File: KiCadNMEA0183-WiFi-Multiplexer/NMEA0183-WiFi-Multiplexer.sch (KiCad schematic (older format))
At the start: 11 parts, among them J1 NMEA In, J2 NMEA In, Q1 BC547, Q2 BC547, U1 WeMos_D1_mini

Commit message: Add files via upload
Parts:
- removed D1, D2: 1N4148, Diode_THT:D_DO-35_SOD27_P7.62mm_Horizontal, symbol Diode:1N4148
- removed Q1, Q2: BC547, Package_TO_SOT_THT:TO-92_Inline, symbol Transistor_BJT:BC547
- removed R1, R2: 33K, symbol Device:R
- removed R3, R4: 10K, symbol Device:R
- added C1, C2, C3, C4: 1µ, symbol Device:CP
- added U2: MAX232, symbol Interface_UART:MAX232
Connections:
- net GND is gone; now on an unnamed net: J1.1 (Pin_1), U1.10 (GND)
- net at U1.6 (MOSI/D7): now also U2.12 (R1OUT)
- net at U1.7 (CS/D8): now also U2.9 (R2OUT)
- net at U1.9 (5V): now also U2.16 (VCC)
- net at J1.2 (Pin_2): now also U2.8 (R2IN)
- net at J2.1 (Pin_1): now also C1.2, C3.1, U2.15 (GND)
- net at J2.2 (Pin_2): now also U2.13 (R1IN)
- new net: C4.1, U2.1 (C1+)
- new net: C1.1, U2.2 (VS+)
- new net: C4.2, U2.3 (C1-)
- new net: C2.1, U2.4 (C2+)
- new net: C2.2, U2.5 (C2-)
- new net: C3.2, U2.6 (VS-)
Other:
- moved on the sheet: J1, J2, U1
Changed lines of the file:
@@
 L MCU_Module:WeMos_D1_mini U1
 U 1 1 604342F8
-P 6100 3950
-F 0 "U1" H 6100 4900 50  0000 C CNN
-F 1 "WeMos_D1_mini" H 6100 5000 50  0000 C CNN
-F 2 "Module:WEMOS_D1_mini_light" H 6100 2800 50  0001 C CNN
-F 3 "https://wiki.wemos.cc/products:d1:d1_mini#documentation" H 4250 2800 50  0001 C CNN
-	1    6100 3950
+P 7050 4100
+F 0 "U1" H 7050 5050 50  0000 C CNN
+F 1 "WeMos_D1_mini" H 7050 5150 50  0000 C CNN
+F 2 "Module:WEMOS_D1_mini_light" H 7050 2950 50  0001 C CNN
+F 3 "https://wiki.wemos.cc/products:d1:d1_mini#documentation" H 5200 2950 50  0001 C CNN
+	1    7050 4100
 	-1   0    0    -1
-$EndComp
-$Comp
-L Transistor_BJT:BC547 Q1
-U 1 1 6043679E
-P 4850 4550
-F 0 "Q1" H 5041 4596 50  0000 L CNN
-F 1 "BC547" H 5041 4505 50  0000 L CNN
-F 2 "Package_TO_SOT_THT:TO-92_Inline" H 5050 4475 50  0001 L CIN
-F 3 "http://www.fairchildsemi.com/ds/BC/BC547.pdf" H 4850 4550 50  0001 L CNN
-	1    4850 4550
-	1    0    0    -1
-$EndComp
-$Comp
-L Device:R R1
-U 1 1 60437DBF
-P 4300 4550
-F 0 "R1" V 4093 4550 50  0000 C CNN
-F 1 "33K" V 4184 4550 50  0000 C CNN
-F 2 "" V 4230 4550 50  0001 C CNN
-F 3 "~" H 4300 4550 50  0001 C CNN
-	1    4300 4550
-	0    1    1    0
 $EndComp
 $Comp
 L Connector_Generic:Conn_01x02 J1
 U 1 1 60439978
-P 3800 4650
-F 0 "J1" H 3718 4325 50  0000 C CNN
-F 1 "NMEA In" H 3718 4416 50  0000 C CNN
-F 2 "" H 3800 4650 50  0001 C CNN
-F 3 "~" H 3800 4650 50  0001 C CNN
-	1    3800 4650
+P 1650 4600
+F 0 "J1" H 1568 4275 50  0000 C CNN
+F 1 "NMEA In" H 1568 4366 50  0000 C CNN
+F 2 "" H 1650 4600 50  0001 C CNN
+F 3 "~" H 1650 4600 50  0001 C CNN
+	1    1650 4600
 	-1   0    0    1
-$EndComp
-Wire Wire Line
-	4000 4550 4150 4550
-Wire Wire Line
-	4950 4350 5700 4350
-Wire Wire Line
-	4450 4550 4550 4550
-Wire Wire Line
-	4550 4650 4550 4550
-Connection ~ 4550 4550
-Wire Wire Line
-	4550 4550 4650 4550
-$Comp
-L power:GND #PWR01
-U 1 1 6043BBF4
-P 6100 4950
-F 0 "#PWR01" H 6100 4700 50  0001 C CNN
-F 1 "GND" H 6105 4777 50  0000 C CNN
-F 2 "" H 6100 4950 50  0001 C CNN
-F 3 "" H 6100 4950 50  0001 C CNN
-	1    6100 4950
-	1    0    0    -1
-$EndComp
-Wire Wire Line
-	6100 4750 6100 4950
-$Comp
-L Device:R R4
-U 1 1 6044381A
-P 4950 4200
-F 0 "R4" H 5020 4246 50  0000 L CNN
-F 1 "10K" H 5020 4155 50  0000 L CNN
-F 2 "" V 4880 4200 50  0001 C CNN
-F 3 "~" H 4950 4200 50  0001 C CNN
-	1    4950 4200
-	1    0    0    -1
-$EndComp
-Connection ~ 4950 4350
-Connection ~ 6100 4950
-$Comp
-L Transistor_BJT:BC547 Q2
-U 1 1 6043EAEA
-P 4850 3450
-F 0 "Q2" H 5041 3496 50  0000 L CNN
-F 1 "BC547" H 5041 3405 50  0000 L CNN
-F 2 "Package_TO_SOT_THT:TO-92_Inline" H 5050 3375 50  0001 L CIN
-F 3 "http://www.fairchildsemi.com/ds/BC/BC547.pdf" H 4850 3450 50  0001 L CNN
-	1    4850 3450
-	1    0    0    -1
-$EndComp
-$Comp
-L Device:R R2
-U 1 1 6043EAF4
-P 4300 3450
-F 0 "R2" V 4093 3450 50  0000 C CNN
-F 1 "33K" V 4184 3450 50  0000 C CNN
-F 2 "" V 4230 3450 50  0001 C CNN
-F 3 "~" H 4300 3450 50  0001 C CNN
-	1    4300 3450
-	0    1    1    0
-$EndComp
-$Comp
-L Diode:1N4148 D1
-U 1 1 6043EAFE
-P 4550 3700
-F 0 "D1" V 4504 3779 50  0000 L CNN
-F 1 "1N4148" V 4595 3779 50  0000 L CNN
-F 2 "Diode_THT:D_DO-35_SOD27_P7.62mm_Horizontal" H 4550 3525 50  0001 C CNN
-F 3 "https://assets.nexperia.com/documents/data-sheet/1N4148_1N4448.pdf" H 4550 3700 50  0001 C CNN
-	1    4550 3700
-	0    1    1    0
 $EndComp
 $Comp
 L Connector_Generic:Conn_01x02 J2
 U 1 1 6043EB08
-P 3800 3550
-F 0 "J2" H 3718 3225 50  0000 C CNN
-F 1 "NMEA In" H 3718 3316 50  0000 C CNN
-F 2 "" H 3800 3550 50  0001 C CNN
-F 3 "~" H 3800 3550 50  0001 C CNN
-	1    3800 3550
+P 1650 3350
+F 0 "J2" H 1568 3025 50  0000 C CNN
+F 1 "NMEA In" H 1568 3116 50  0000 C CNN
+F 2 "" H 1650 3350 50  0001 C CNN
+F 3 "~" H 1650 3350 50  0001 C CNN
+	1    1650 3350
 	-1   0    0    1
 $EndComp
 Wire Wire Line
-	4000 3450 4150 3450
+	5150 4300 5950 4300
 Wire Wire Line
-	4000 3550 4000 3850
+	5950 4300 5950 4400
 Wire Wire Line
-	4000 3850 4550 3850
+	5950 4400 6650 4400
 Wire Wire Line
-	4950 3650 4950 3850
-Connection ~ 4550 3850
-Wire Wire Line
-	4450 3450 4550 3450
-Wire Wire Line
-	4550 3850 4950 3850
-Wire Wire Line
-	4550 3550 4550 3450
-Connection ~ 4550 3450
-Wire Wire Line
-	4550 3450 4650 3450
-Wire Wire Line
-	4950 4950 6100 4950
-Wire Wire Line
-	4550 4950 4950 4950
-Connection ~ 4550 4950
-Connection ~ 4950 4950
-Wire Wire Line
-	4950 4750 4950 4950
-Wire Wire Line
-	4000 4950 4550 4950
-Wire Wire Line
-	4000 4650 4000 4950
+	5150 4500 6650 4500
 $Comp
-L Diode:1N4148 D2
-U 1 1 60438826
-P 4550 4800
-F 0 "D2" V 4504 4879 50  0000 L CNN
-F 1 "1N4148" V 4595 4879 50  0000 L CNN
-F 2 "Diode_THT:D_DO-35_SOD27_P7.62mm_Horizontal" H 4550 4625 50  0001 C CNN
-F 3 "https://assets.nexperia.com/documents/data-sheet/1N4148_1N4448.pdf" H 4550 4800 50  0001 C CNN
-	1    4550 4800
-	0    1    1    0
+L Device:CP C2
+U 1 1 6043F041
+P 3200 3050
+F 0 "C2" H 3318 3096 50  0000 L CNN
+F 1 "1µ" H 3318 3005 50  0000 L CNN
+F 2 "" H 3238 2900 50  0001 C CNN
+F 3 "~" H 3200 3050 50  0001 C CNN
+	1    3200 3050
+	1    0    0    -1
 $EndComp
 $Comp
-L Device:R R3
-U 1 1 6044AD30
-P 4950 3100
-F 0 "R3" H 5020 3146 50  0000 L CNN
-F 1 "10K" H 5020 3055 50  0000 L CNN
-F 2 "" V 4880 3100 50  0001 C CNN
-F 3 "~" H 4950 3100 50  0001 C CNN
-	1    4950 3100
+L Device:CP C4
+U 1 1 6043FA82
+P 5450 3050
+F 0 "C4" H 5568 3096 50  0000 L CNN
+F 1 "1µ" H 5568 3005 50  0000 L CNN
+F 2 "" H 5488 2900 50  0001 C CNN
+F 3 "~" H 5450 3050 50  0001 C CNN
+	1    5450 3050
 	1    0    0    -1
 $EndComp
 Wire Wire Line
-	4950 2950 5450 2950
+	3200 2900 3550 2900
 Wire Wire Line
-	5450 2950 5450 3150
+	3200 3200 3550 3200
 Wire Wire Line
-	5450 3150 6000 3150
+	5150 2900 5450 2900
 Wire Wire Line
-	4950 4050 5450 4050
+	5150 3200 5450 3200
+$Comp
+L Device:CP C1
+U 1 1 604409F9
+P 2800 3650
+F 0 "C1" H 2918 3696 50  0000 L CNN
+F 1 "1µ" H 2918 3605 50  0000 L CNN
+F 2 "" H 2838 3500 50  0001 C CNN
+F 3 "~" H 2800 3650 50  0001 C CNN
+	1    2800 3650
+	1    0    0    -1
+$EndComp
+$Comp
+L Device:CP C3
+U 1 1 60441930
+P 3200 3650
+F 0 "C3" H 3082 3604 50  0000 R CNN
+F 1 "1µ" H 3082 3695 50  0000 R CNN
+F 2 "" H 3238 3500 50  0001 C CNN
+F 3 "~" H 3200 3650 50  0001 C CNN
+	1    3200 3650
+	-1   0    0    1
+$EndComp
 Wire Wire Line
-	5450 4050 5450 3150
-Connection ~ 5450 3150
+	2800 3500 2800 3400
 Wire Wire Line
-	4950 3250 5250 3250
+	2800 3400 3550 3400
 Wire Wire Line
-	5250 3250 5250 4250
+	3200 3500 3550 3500
 Wire Wire Line
-	5250 4250 5700 4250
-Connection ~ 4950 3250
+	3550 3500 3550 3700
+Wire Wire Line
+	1850 3350 1850 3800
+Wire Wire Line
+	1850 3800 2800 3800
+Connection ~ 2800 3800
+Wire Wire Line
+	1850 4600 2800 4600
+Wire Wire Line
+	2800 5150 4350 5150
+Wire Wire Line
+	4350 5150 4350 5000
+Wire Wire Line
+	4350 5150 7050 5150
+Wire Wire Line
+	7050 5150 7050 4900
+Connection ~ 4350 5150
+Wire Wire Line
+	7150 3300 7150 3200
+Wire Wire Line
+	7150 3200 6150 3200
+Wire Wire Line
+	6150 3200 6150 2600
+Wire Wire Line
+	6150 2600 4350 2600
+Connection ~ 2800 4600
+Wire Wire Line
+	2800 4600 2800 5150
+Wire Wire Line
+	2800 3800 2800 4600
+Wire Wire Line
+	1850 4500 3550 4500
+Wire Wire Line
+	1850 3250 2450 3250
+Wire Wire Line
+	2450 3250 2450 4300
+Wire Wire Line
+	2450 4300 3550 4300
+Wire Wire Line
+	2800 3800 3200 3800
+$Comp
+L Interface_UART:MAX232 U2
+U 1 1 60437BD0
+P 4350 3800
+F 0 "U2" H 4350 5181 50  0000 C CNN
+F 1 "MAX232" H 4350 5090 50  0000 C CNN
+F 2 "" H 4400 2750 50  0001 L CNN
+F 3 "http://www.ti.com/lit/ds/symlink/max232.pdf" H 4350 3900 50  0001 C CNN
+	1    4350 3800
+	-1   0    0    -1
+$EndComp
 $EndSCHEMATC

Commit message: Add files via upload
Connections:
- net GND: now reaches C1.2, C3.1, J1.1 (Pin_1), J2.1 (Pin_1), U1.10 (GND), U2.15 (GND)
- net +5V: now reaches U1.9 (5V), U2.16 (VCC)
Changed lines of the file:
@@
 	-1   0    0    -1
 $EndComp
+$Comp
+L power:+5V #PWR?
+U 1 1 60437FA3
+P 6150 2600
+F 0 "#PWR?" H 6150 2450 50  0001 C CNN
+F 1 "+5V" H 6165 2773 50  0000 C CNN
+F 2 "" H 6150 2600 50  0001 C CNN
+F 3 "" H 6150 2600 50  0001 C CNN
+	1    6150 2600
+	1    0    0    -1
+$EndComp
+Connection ~ 6150 2600
+$Comp
+L power:GND #PWR?
+U 1 1 60438682
+P 4350 5150
+F 0 "#PWR?" H 4350 4900 50  0001 C CNN
+F 1 "GND" H 4355 4977 50  0000 C CNN
+F 2 "" H 4350 5150 50  0001 C CNN
+F 3 "" H 4350 5150 50  0001 C CNN
+	1    4350 5150
+	1    0    0    -1
+$EndComp
 $EndSCHEMATC

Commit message: Add files via upload
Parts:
- renumbered J2 to J1, J1 to J2
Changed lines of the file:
@@
 $EndComp
 $Comp
-L Connector_Generic:Conn_01x02 J1
+L Connector_Generic:Conn_01x02 J2
 U 1 1 60439978
 P 1650 4600
-F 0 "J1" H 1568 4275 50  0000 C CNN
+F 0 "J2" H 1568 4275 50  0000 C CNN
 F 1 "NMEA In" H 1568 4366 50  0000 C CNN
 F 2 "" H 1650 4600 50  0001 C CNN
@@
 $EndComp
 $Comp
-L Connector_Generic:Conn_01x02 J2
+L Connector_Generic:Conn_01x02 J1
 U 1 1 6043EB08
 P 1650 3350
-F 0 "J2" H 1568 3025 50  0000 C CNN
+F 0 "J1" H 1568 3025 50  0000 C CNN
 F 1 "NMEA In" H 1568 3116 50  0000 C CNN
 F 2 "" H 1650 3350 50  0001 C CNN

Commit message: Add files via upload
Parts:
- C1, C2, C3, C4: footprint (none) -> Capacitor_THT:CP_Radial_D6.3mm_P2.50mm
- J1, J2: footprint (none) -> TerminalBlock:TerminalBlock_bornier-2_P5.08mm
- U2: footprint (none) -> Package_DIP:DIP-16_W7.62mm_Socket
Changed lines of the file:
@@
 F 0 "J2" H 1568 4275 50  0000 C CNN
 F 1 "NMEA In" H 1568 4366 50  0000 C CNN
-F 2 "" H 1650 4600 50  0001 C CNN
+F 2 "TerminalBlock:TerminalBlock_bornier-2_P5.08mm" H 1650 4600 50  0001 C CNN
 F 3 "~" H 1650 4600 50  0001 C CNN
 	1    1650 4600
@@
 F 0 "J1" H 1568 3025 50  0000 C CNN
 F 1 "NMEA In" H 1568 3116 50  0000 C CNN
-F 2 "" H 1650 3350 50  0001 C CNN
+F 2 "TerminalBlock:TerminalBlock_bornier-2_P5.08mm" H 1650 3350 50  0001 C CNN
 F 3 "~" H 1650 3350 50  0001 C CNN
 	1    1650 3350
@@
 F 0 "C2" H 3318 3096 50  0000 L CNN
 F 1 "1µ" H 3318 3005 50  0000 L CNN
-F 2 "" H 3238 2900 50  0001 C CNN
+F 2 "Capacitor_THT:CP_Radial_D6.3mm_P2.50mm" H 3238 2900 50  0001 C CNN
 F 3 "~" H 3200 3050 50  0001 C CNN
 	1    3200 3050
@@
 F 0 "C4" H 5568 3096 50  0000 L CNN
 F 1 "1µ" H 5568 3005 50  0000 L CNN
-F 2 "" H 5488 2900 50  0001 C CNN
+F 2 "Capacitor_THT:CP_Radial_D6.3mm_P2.50mm" H 5488 2900 50  0001 C CNN
 F 3 "~" H 5450 3050 50  0001 C CNN
 	1    5450 3050
@@
 F 0 "C1" H 2918 3696 50  0000 L CNN
 F 1 "1µ" H 2918 3605 50  0000 L CNN
-F 2 "" H 2838 3500 50  0001 C CNN
+F 2 "Capacitor_THT:CP_Radial_D6.3mm_P2.50mm" H 2838 3500 50  0001 C CNN
 F 3 "~" H 2800 3650 50  0001 C CNN
 	1    2800 3650
@@
 F 0 "C3" H 3082 3604 50  0000 R CNN
 F 1 "1µ" H 3082 3695 50  0000 R CNN
-F 2 "" H 3238 3500 50  0001 C CNN
+F 2 "Capacitor_THT:CP_Radial_D6.3mm_P2.50mm" H 3238 3500 50  0001 C CNN
 F 3 "~" H 3200 3650 50  0001 C CNN
 	1    3200 3650
@@
 F 0 "U2" H 4350 5181 50  0000 C CNN
 F 1 "MAX232" H 4350 5090 50  0000 C CNN
-F 2 "" H 4400 2750 50  0001 L CNN
+F 2 "Package_DIP:DIP-16_W7.62mm_Socket" H 4400 2750 50  0001 L CNN
 F 3 "http://www.ti.com/lit/ds/symlink/max232.pdf" H 4350 3900 50  0001 C CNN
 	1    4350 3800
@@
 $EndComp
 $Comp
-L power:+5V #PWR?
+L power:+5V #PWR0101
 U 1 1 60437FA3
 P 6150 2600
-F 0 "#PWR?" H 6150 2450 50  0001 C CNN
+F 0 "#PWR0101" H 6150 2450 50  0001 C CNN
 F 1 "+5V" H 6165 2773 50  0000 C CNN
 F 2 "" H 6150 2600 50  0001 C CNN
@@
 Connection ~ 6150 2600
 $Comp
-L power:GND #PWR?
+L power:GND #PWR0102
 U 1 1 60438682
 P 4350 5150
-F 0 "#PWR?" H 4350 4900 50  0001 C CNN
+F 0 "#PWR0102" H 4350 4900 50  0001 C CNN
 F 1 "GND" H 4355 4977 50  0000 C CNN
 F 2 "" H 4350 5150 50  0001 C CNN

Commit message: Add files via upload
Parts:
- added J3: Power, TerminalBlock:TerminalBlock_bornier-2_P5.08mm, symbol Connector_Generic:Conn_01x02
- added U3: R-78E50-10_TO220, Package_TO_SOT_THT:TO-220-3_Vertical, symbol Regulator_Linear:LM7805_TO220
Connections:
- net +5V: now also U3.3 (VO)
- net GND: now also J3.1 (Pin_1), U3.2 (GND)
- new net: J3.2 (Pin_2), U3.1 (VI)
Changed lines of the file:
@@
 	1850 3350 1850 3800
 Wire Wire Line
-	1850 3800 2800 3800
+	1850 3800 2600 3800
 Connection ~ 2800 3800
 Wire Wire Line
@@
 	1    0    0    -1
 $EndComp
+$Comp
+L Connector_Generic:Conn_01x02 J3
+U 1 1 6044E52D
+P 1650 2600
+F 0 "J3" H 1568 2275 50  0000 C CNN
+F 1 "Power" H 1568 2366 50  0000 C CNN
+F 2 "TerminalBlock:TerminalBlock_bornier-2_P5.08mm" H 1650 2600 50  0001 C CNN
+F 3 "~" H 1650 2600 50  0001 C CNN
+	1    1650 2600
+	-1   0    0    1
+$EndComp
+$Comp
+L Regulator_Linear:LM7805_TO220 U3
+U 1 1 6044EDD0
+P 2400 2500
+F 0 "U3" H 2400 2742 50  0000 C CNN
+F 1 "R-78E50-10_TO220" H 2400 2651 50  0000 C CNN
+F 2 "Package_TO_SOT_THT:TO-220-3_Vertical" H 2400 2725 50  0001 C CIN
+F 3 "http://www.fairchildsemi.com/ds/LM/LM7805.pdf" H 2400 2450 50  0001 C CNN
+	1    2400 2500
+	1    0    0    -1
+$EndComp
+Wire Wire Line
+	1850 2500 2100 2500
+Wire Wire Line
+	2400 2800 2600 2800
+Wire Wire Line
+	2600 2800 2600 3800
+Connection ~ 2600 3800
+Wire Wire Line
+	2600 3800 2800 3800
+Wire Wire Line
+	2700 2500 3400 2500
+Wire Wire Line
+	3400 2500 3400 2600
+Wire Wire Line
+	3400 2600 4350 2600
+Connection ~ 4350 2600
+Wire Wire Line
+	1850 2600 1850 2800
+Wire Wire Line
+	1850 2800 2400 2800
+Connection ~ 2400 2800
 $EndSCHEMATC

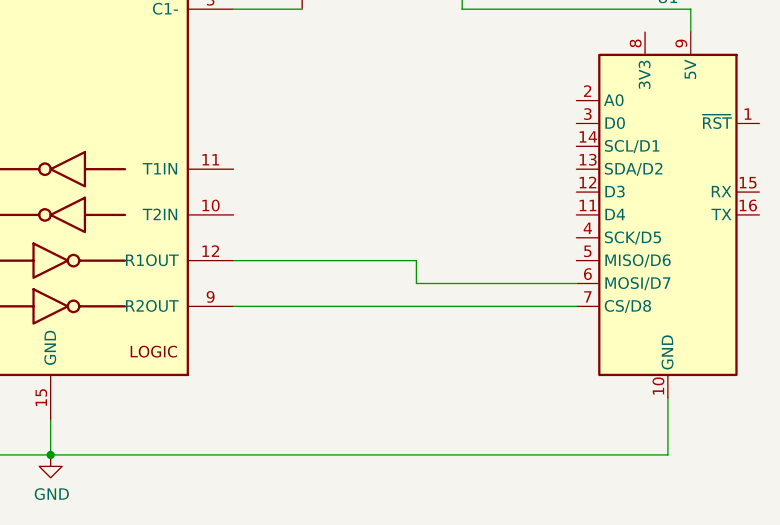
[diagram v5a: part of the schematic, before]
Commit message: Version 1.1 (Changed to D7/D2 pins to avoid boot problems).
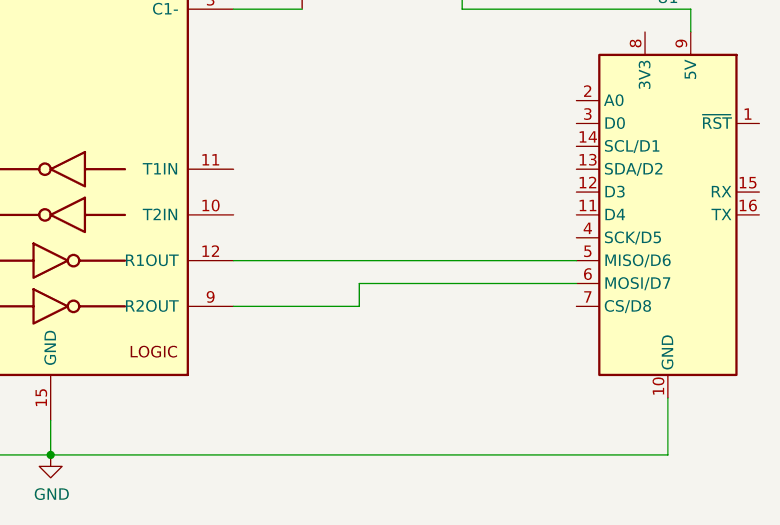
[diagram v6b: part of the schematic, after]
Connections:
- net at U1.5 (MISO/D6): now also U2.12 (R1OUT)
- net at U1.6 (MOSI/D7): now also U2.9 (R2OUT); no longer U2.12 (R1OUT)
- net at U1.7 (CS/D8): no longer U2.9 (R2OUT)
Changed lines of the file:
@@
 	-1   0    0    1
 $EndComp
-Wire Wire Line
-	5150 4300 5950 4300
-Wire Wire Line
-	5950 4300 5950 4400
-Wire Wire Line
-	5950 4400 6650 4400
-Wire Wire Line
-	5150 4500 6650 4500
 $Comp
 L Device:CP C2
@@
 	1850 2800 2400 2800
 Connection ~ 2400 2800
+Wire Wire Line
+	5150 4300 6650 4300
+Wire Wire Line
+	5150 4500 5700 4500
+Wire Wire Line
+	5700 4500 5700 4400
+Wire Wire Line
+	5700 4400 6650 4400
 $EndSCHEMATC
